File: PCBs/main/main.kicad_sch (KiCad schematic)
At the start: 6 parts, among them J1 chambers 03-04, J2 chambers 01-02, J3 chambers 05-06, J4 chambers 07-08, J5 chambers 9-10

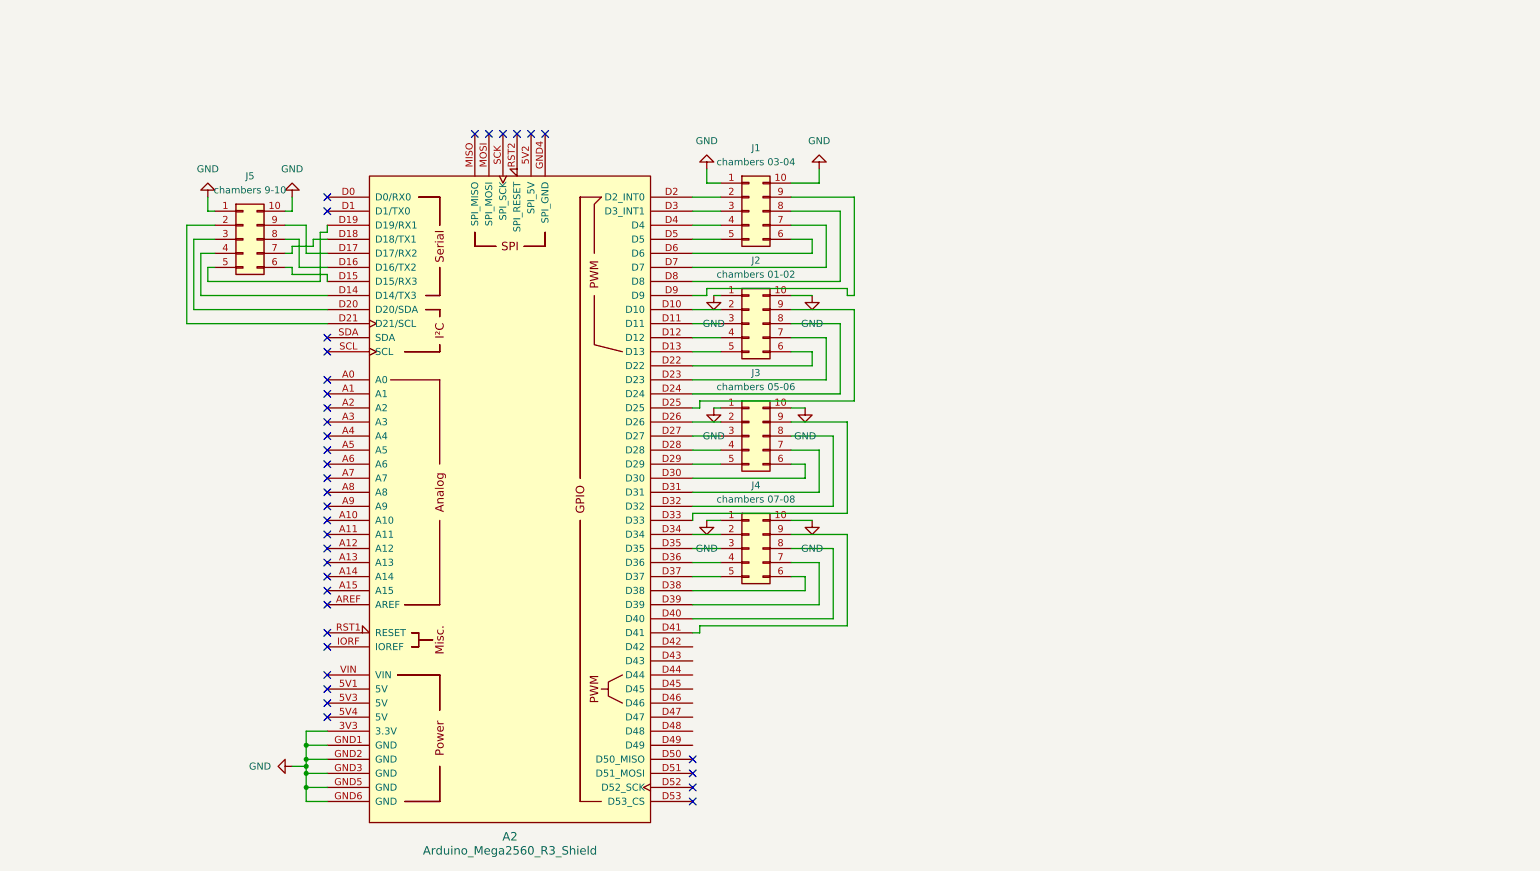
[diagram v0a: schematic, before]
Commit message: create PCBs for easier replication of the system. It has been altered to use an arduino Mega, instead of an arduino Uno.
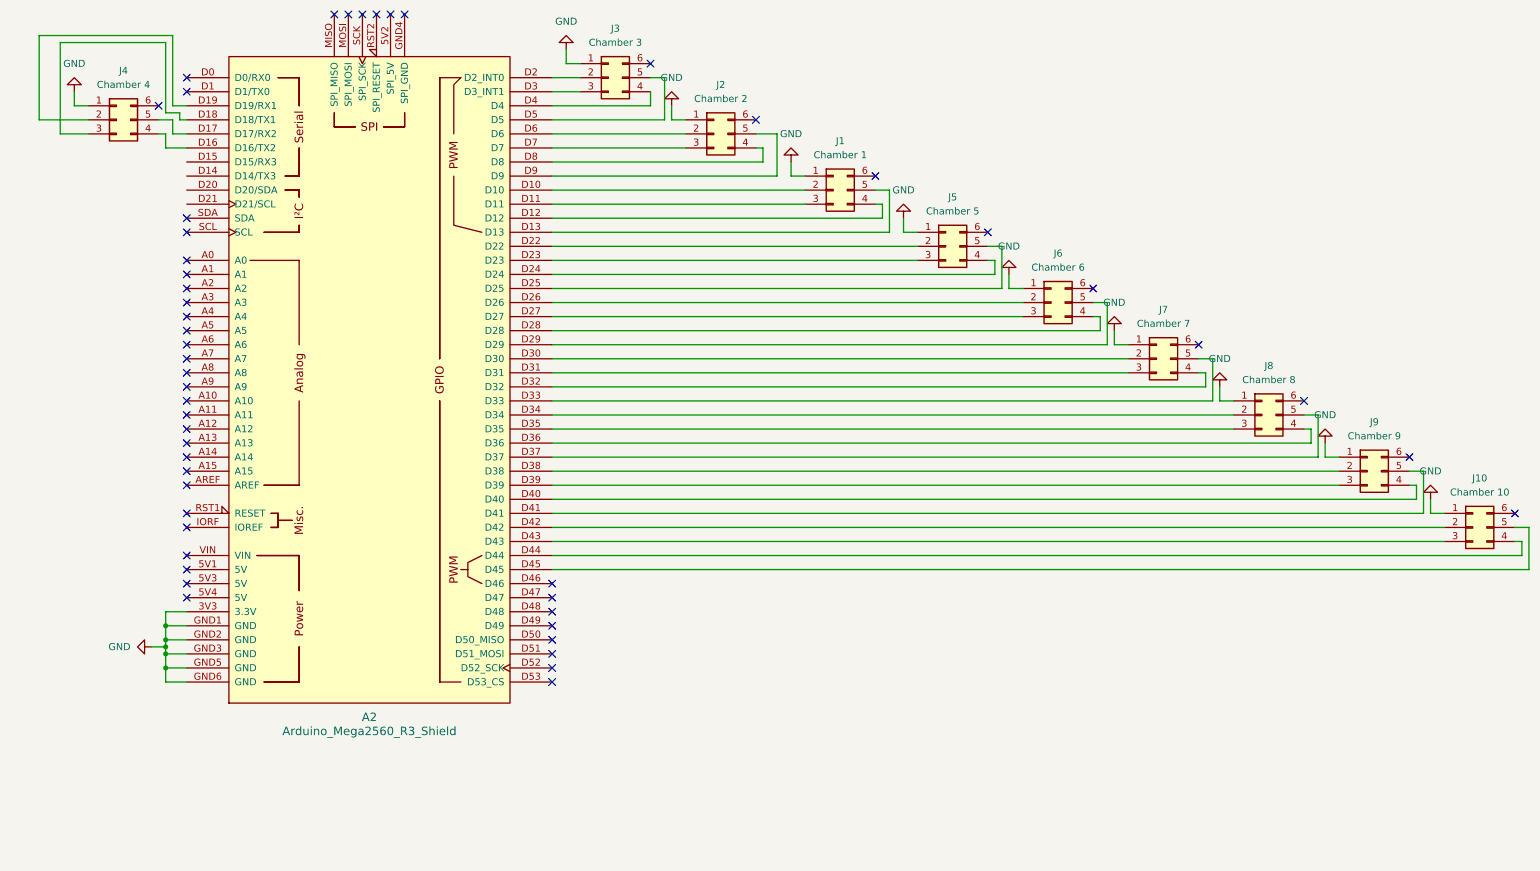
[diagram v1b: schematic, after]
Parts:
- removed J1: chambers 03-04, Connector_IDC:IDC-Header_2x05_P2.54mm_Vertical, symbol Connector_Generic:Conn_02x05_Counter_Clockwise
- removed J2: chambers 01-02, Connector_IDC:IDC-Header_2x05_P2.54mm_Vertical, symbol Connector_Generic:Conn_02x05_Counter_Clockwise
- removed J3: chambers 05-06, Connector_IDC:IDC-Header_2x05_P2.54mm_Vertical, symbol Connector_Generic:Conn_02x05_Counter_Clockwise
- removed J4: chambers 07-08, Connector_IDC:IDC-Header_2x05_P2.54mm_Vertical, symbol Connector_Generic:Conn_02x05_Counter_Clockwise
- removed J5: chambers 9-10, Connector_IDC:IDC-Header_2x05_P2.54mm_Vertical, symbol Connector_Generic:Conn_02x05_Counter_Clockwise
- added J1: Chamber 1, Connector_IDC:IDC-Header_2x03_P2.54mm_Vertical, symbol Connector_Generic:Conn_02x03_Counter_Clockwise
- added J10: Chamber 10, Connector_IDC:IDC-Header_2x03_P2.54mm_Vertical, symbol Connector_Generic:Conn_02x03_Counter_Clockwise
- added J2: Chamber 2, Connector_IDC:IDC-Header_2x03_P2.54mm_Vertical, symbol Connector_Generic:Conn_02x03_Counter_Clockwise
- added J3: Chamber 3, Connector_IDC:IDC-Header_2x03_P2.54mm_Vertical, symbol Connector_Generic:Conn_02x03_Counter_Clockwise
- added J4: Chamber 4, Connector_IDC:IDC-Header_2x03_P2.54mm_Vertical, symbol Connector_Generic:Conn_02x03_Counter_Clockwise
- added J5: Chamber 5, Connector_IDC:IDC-Header_2x03_P2.54mm_Vertical, symbol Connector_Generic:Conn_02x03_Counter_Clockwise
- added J6: Chamber 6, Connector_IDC:IDC-Header_2x03_P2.54mm_Vertical, symbol Connector_Generic:Conn_02x03_Counter_Clockwise
- added J7: Chamber 7, Connector_IDC:IDC-Header_2x03_P2.54mm_Vertical, symbol Connector_Generic:Conn_02x03_Counter_Clockwise
- added J8: Chamber 8, Connector_IDC:IDC-Header_2x03_P2.54mm_Vertical, symbol Connector_Generic:Conn_02x03_Counter_Clockwise
- added J9: Chamber 9, Connector_IDC:IDC-Header_2x03_P2.54mm_Vertical, symbol Connector_Generic:Conn_02x03_Counter_Clockwise
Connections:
- net GND: now also J1.1 (Pin_1), J10.1 (Pin_1), J2.1 (Pin_1), J3.1 (Pin_1), J4.1 (Pin_1), J5.1 (Pin_1), J6.1 (Pin_1), J7.1 (Pin_1), J8.1 (Pin_1), J9.1 (Pin_1)
- net at A2.D26: now also J6.2 (Pin_2)
- net at A2.D27: now also J6.3 (Pin_3)
- net at A2.D28: now also J6.4 (Pin_4)
- net at A2.D29: now also J6.5 (Pin_5)
- net at A2.D30: now also J7.2 (Pin_2)
- net at A2.D31: now also J7.3 (Pin_3)
- net at A2.D32: now also J7.4 (Pin_4)
- net at A2.D33: now also J7.5 (Pin_5)
- net at A2.D10: now also J1.2 (Pin_2)
- net at A2.D11: now also J1.3 (Pin_3)
- net at A2.D12: now also J1.4 (Pin_4)
- net at A2.D13: now also J1.5 (Pin_5)
- net at A2.D22: now also J5.2 (Pin_2)
- net at A2.D23: now also J5.3 (Pin_3)
- net at A2.D24: now also J5.4 (Pin_4)
- net at A2.D25: now also J5.5 (Pin_5)
- net at A2.D19 (D19/RX1): now also J4.2 (Pin_2)
- net at A2.D18 (D18/TX1): now also J4.3 (Pin_3)
- net at A2.D16 (D16/TX2): now also J4.4 (Pin_4)
- net at A2.D17 (D17/RX2): now also J4.5 (Pin_5)
- net at A2.D2 (D2_INT0): now also J3.2 (Pin_2)
- net at A2.D3 (D3_INT1): now also J3.3 (Pin_3)
- net at A2.D34: now also J8.2 (Pin_2)
- net at A2.D35: now also J8.3 (Pin_3)
- net at A2.D36: now also J8.4 (Pin_4)
- net at A2.D37: now also J8.5 (Pin_5)
- net at A2.D38: now also J9.2 (Pin_2)
- net at A2.D39: now also J9.3 (Pin_3)
- net at A2.D4: now also J3.4 (Pin_4)
- net at A2.D40: now also J9.4 (Pin_4)
- net at A2.D41: now also J9.5 (Pin_5)
- net at A2.D42: now also J10.2 (Pin_2)
- net at A2.D43: now also J10.3 (Pin_3)
- net at A2.D44: now also J10.4 (Pin_4)
- net at A2.D45: now also J10.5 (Pin_5)
- net at A2.D5: now also J3.5 (Pin_5)
- net at A2.D6: now also J2.2 (Pin_2)
- net at A2.D7: now also J2.3 (Pin_3)
- net at A2.D8: now also J2.4 (Pin_4)
- net at A2.D9: now also J2.5 (Pin_5)
- no-connect marks 37 -> 51
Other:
- moved on the sheet: A2

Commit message: polish main pcb
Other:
- note added: "BLUES: D4, D8, D12, D16, D24, D28, D32, D36, D40, D44"
- note added: "Connector map: 1 - GND 2 - RED 3 - GREEN 4 - BLUE 5 - Indicator RED 6 - NC"
- note added: "GREENS: D3, D7, D11, D18, D23, D27, D31, D35, D39, D43"
- note added: "Indicator RED: D5, D9, D13, D17, D25, D29, D32, D37, D41, D45"
- note added: "REDS: D2, D6, D10, D19, D22, D26, D30, D34, D38, D42"
- moved on the sheet: A2, J1, J10, J2, J3, J4, J5, J6, J7, J8, J9
